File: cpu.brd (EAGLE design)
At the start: 94 x 46.5 mm, 87 parts, among them U1 STM32L151R8T6, X1 ED060SC4_EINK, X2 PIIKKIRIMA-5, X3 PIIKKIRIMA-2, X4 629105136821, X5 693071010811, X6 PIIKKIRIMA-6, X7 PIIKKIRIMA-2, X8 PIIKKIRIMA-2, X9 PIIKKIRIMA-2

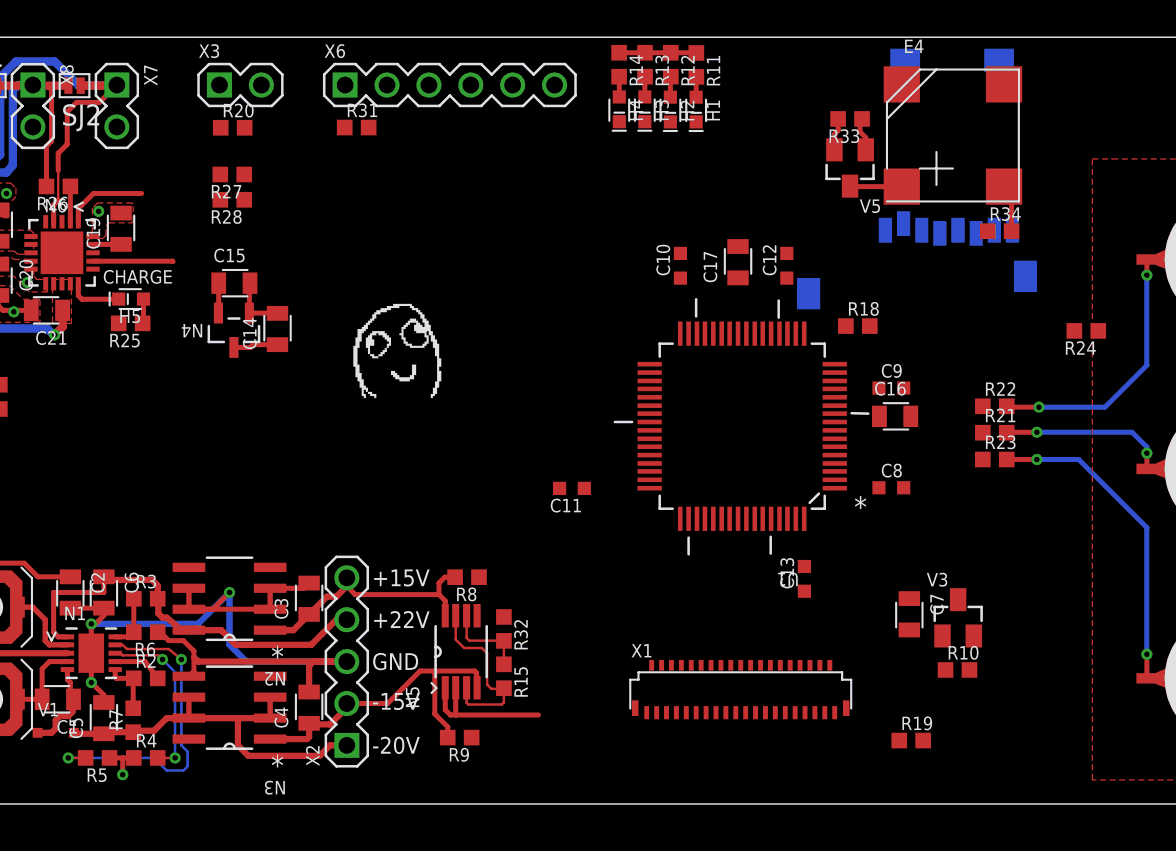
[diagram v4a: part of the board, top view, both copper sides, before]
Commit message: Layout cont
Flex connector first routing attempt. not nice. too many vias...
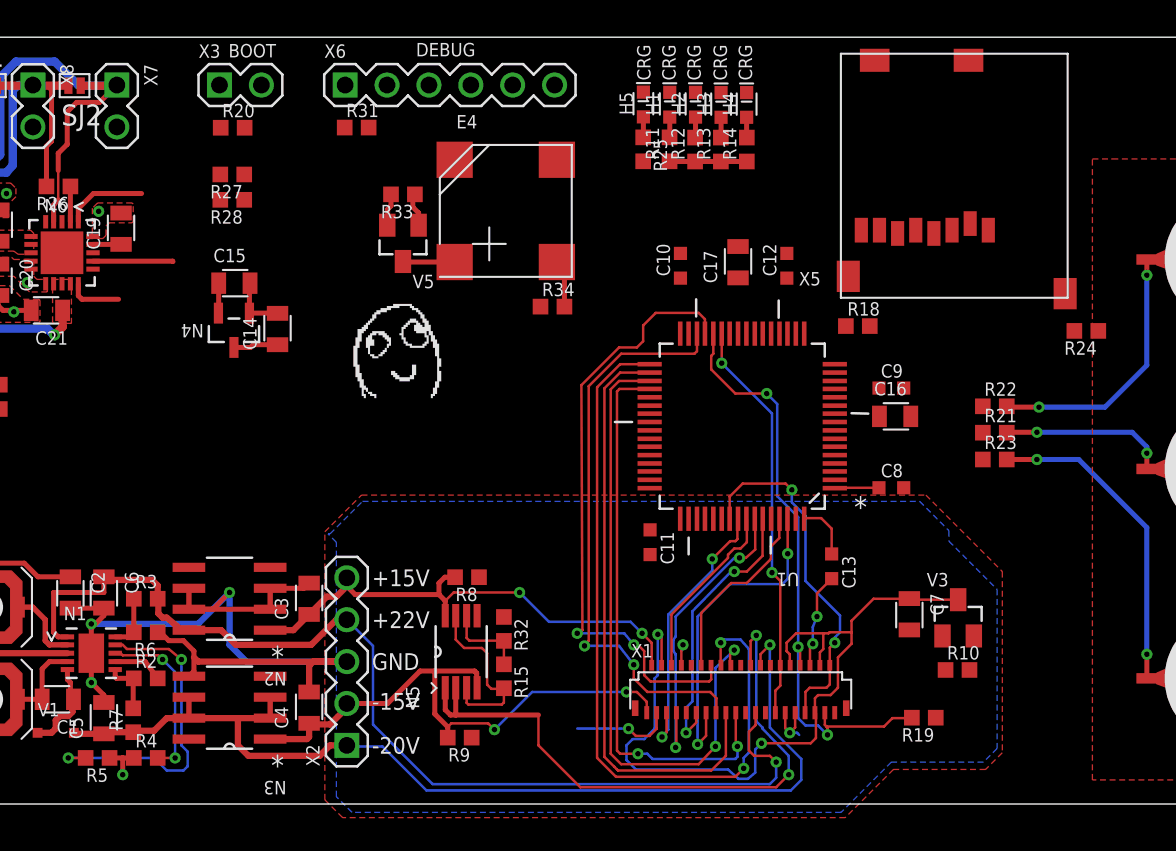
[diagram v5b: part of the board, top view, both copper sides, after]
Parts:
- moved H5 33.2 mm to (58.4, 45.0), turned to 90 degrees
- moved R25 32.8 mm to (58.4, 42.2), turned to 270 degrees
- moved R34 27.5 mm to (52.9, 32.7)
- moved R33 27.5 mm to (43.8, 39.5)
- moved V5 27.5 mm to (43.8, 36.5)
- moved E4 27.5 mm to (50.0, 38.5)
- moved R14 9.30 mm to (64.6, 42.2), turned to 90 degrees
- moved H4 7.73 mm to (64.6, 44.9), turned to 90 degrees
- moved R13 6.90 mm to (63.1, 42.2), turned to 90 degrees
- moved X5 6.24 mm to (79.3, 37.3), flipped to the top
- moved C11 5.75 mm to (58.8, 18.4), turned to 270 degrees
- moved R11 5.37 mm to (60.0, 42.2), turned to 90 degrees
- moved R12 5.35 mm to (61.5, 42.2), turned to 90 degrees
- moved H3 4.63 mm to (63.1, 44.9), turned to 90 degrees
- moved C13 1.82 mm to (69.8, 17.0), turned to 270 degrees
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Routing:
- net VEINK33: track 0.00 -> 47.8 mm, vias 0 -> 2
- net EINKD4: track 0.00 -> 46.6 mm, vias 0 -> 2
- net VNEG20: track 23.6 -> 63.1 mm, vias 0 -> 1
- net EINKD6: track 0.00 -> 39.1 mm, vias 0 -> 2
- net VPOS22: track 26.6 -> 65.0 mm, vias 0 -> 1
- net EINKD2: track 0.00 -> 37.3 mm, vias 0 -> 2
- net SPV/BOOT1: track 0.00 -> 36.8 mm, vias 0 -> 3
- net EINKD5: track 0.00 -> 36.2 mm
- net EINKD3: track 0.00 -> 35.1 mm, vias 0 -> 2
- net EINKD7: track 0.00 -> 34.1 mm, vias 0 -> 2
- net VEINKVCOM: track 8.77 -> 38.3 mm, vias 0 -> 2
- net GMODE: track 0.00 -> 24.6 mm, vias 0 -> 2
- net CKV: track 0.00 -> 21.8 mm, vias 0 -> 2
- net EINKD1: track 0.00 -> 19.9 mm, vias 0 -> 2
- net OE: track 0.00 -> 18.5 mm, vias 0 -> 2
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- added copper zone on layer 16, net GND
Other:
- board text added: "BOOT"
- board text added: "CRG"
- board text added: "DEBUG"
- board text removed: "CHARGE"

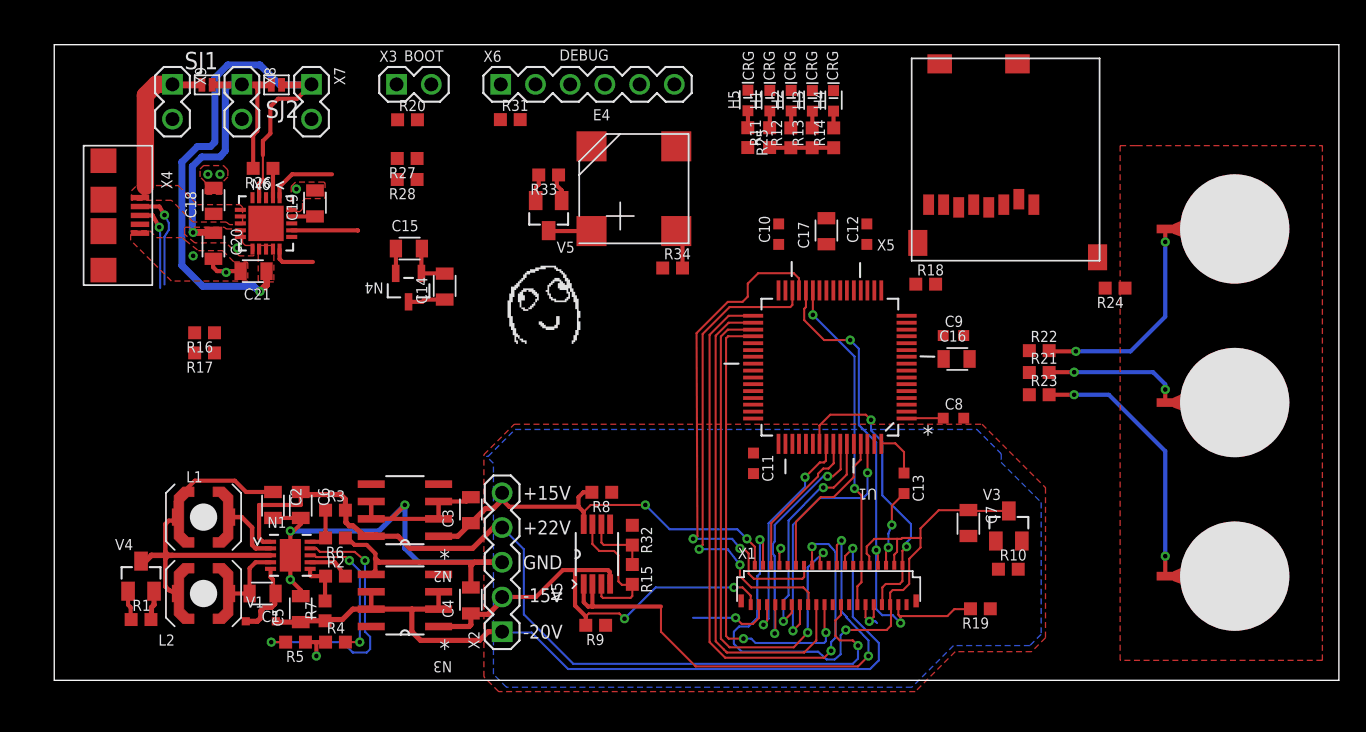
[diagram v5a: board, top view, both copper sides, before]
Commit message: Layout cont2
17 airwires left.
touch buttons removed from cpu board
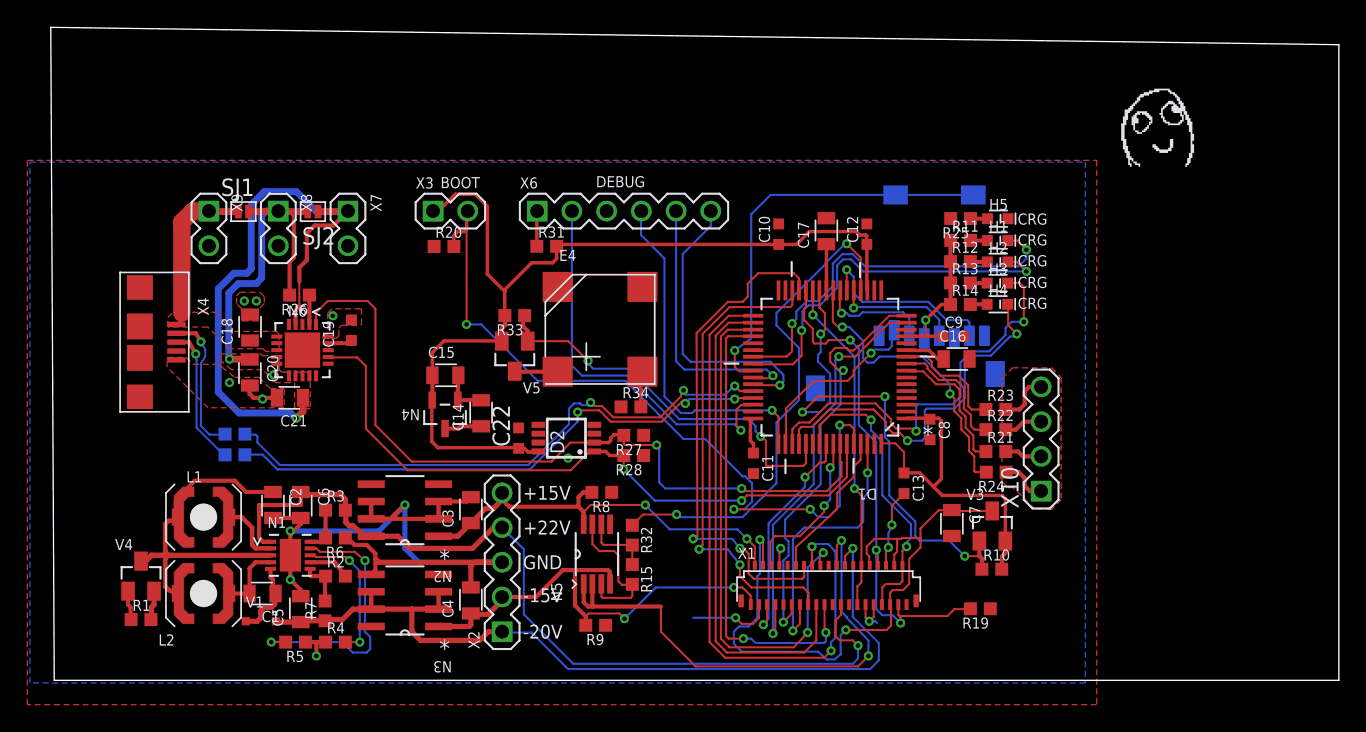
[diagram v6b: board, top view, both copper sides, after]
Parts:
- removed E1, E2, E3: TB_ROUND, OMAT_IC:TB_8MM_ROUND
- removed R18: 22R, rcl:R0603
- added C22: (no value), rcl:C0603
- added D2: TMP75DGK, ti_tmp:MSOP8
- added X10: PIIKKIRIMA-4, OMAT_IC:PIIKKIRIMA-4
- C19: device rcl:C0805 -> rcl:C0603
- moved U$2 46.7 mm to (88.5, 42.7)
- moved R27 26.2 mm to (50.0, 20.5)
- moved R28 26.1 mm to (50.0, 19.0)
- moved H5 20.2 mm to (76.6, 36.3), turned to 0 degrees
- moved H1 19.6 mm to (76.6, 34.7), turned to 0 degrees
- moved H2 19.2 mm to (76.6, 33.1), turned to 0 degrees
- moved H4 19.1 mm to (76.6, 30.0), turned to 0 degrees
- moved H3 19.0 mm to (76.6, 31.6), turned to 0 degrees
- moved R25 16.7 mm to (73.9, 36.3), turned to 180 degrees
- moved R24 16.0 mm to (76.5, 17.8)
- moved R11 15.9 mm to (73.9, 34.7), turned to 0 degrees
- moved R12 15.4 mm to (73.9, 33.2), turned to 0 degrees
- moved R14 15.3 mm to (73.9, 30.0), turned to 0 degrees
- moved R13 15.2 mm to (73.9, 31.6), turned to 0 degrees
- moved X5 14.8 mm to (68.0, 27.7), flipped to the bottom
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- renumbered U1 to D1
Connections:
- net N$12 renamed LED1
- net N$14 renamed LED2
- net N$16 renamed LED3
- net N$19 renamed LED4
- removed net STSCK1: D1.21, R18.1
- net +3V3: now also C22.1, D2.8
- net GND: now also C22.2, D2.4, D2.5, D2.6, D2.7
- net OE: now also D1.15; no longer D1.58
- net SCK1: now also D1.21; no longer R18.2
- net SCL: now also D1.58, D2.2
- net SDA: now also D1.59, D2.1
- net SPH: now also D1.16; no longer D1.59
- net TB1: now also X10.2; no longer E1.1
- net TB2: now also X10.3; no longer E2.1
- net TB3: now also X10.4; no longer E3.1
- net TBSHIELD: now also X10.1
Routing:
- net +3V3: track 14.6 -> 108.2 mm, vias 0 -> 1
- net BOOT0: track 0.00 -> 55.3 mm, vias 0 -> 4
- net SCL: track 5.01 -> 56.8 mm, vias 0 -> 2
- net SDA: track 4.86 -> 49.9 mm, vias 0 -> 2
- net USBDM: track 0.00 -> 43.1 mm, vias 0 -> 3
- net USBDP: track 0.00 -> 41.0 mm, vias 0 -> 3
- net DACOUT1: track 0.00 -> 36.9 mm, vias 0 -> 2
- net EINKVDDCTRLN: track 0.00 -> 36.3 mm, vias 0 -> 4
- net USD_DETN: track 0.00 -> 30.1 mm, vias 0 -> 1
- net LED3: track 0.00 -> 29.9 mm, vias 0 -> 2
- net SWDIO: track 0.00 -> 28.6 mm, vias 0 -> 1
- net LED1: track 0.00 -> 28.5 mm, vias 0 -> 2
- net LED2: track 0.00 -> 28.0 mm, vias 0 -> 2
- net LED4: track 0.00 -> 27.1 mm, vias 0 -> 2
- net BUZCTRLN: track 2.07 -> 29.1 mm, vias 0 -> 2
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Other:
- board size 94 x 46.5 mm -> 94.2 x 47.8 mm

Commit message: Layout complete
First completed layout , Airwires 0
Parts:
- moved U$2 66.5 mm to (23.8, 27.2)
- moved R1 12.6 mm to (2.86, 12.8), turned to 180 degrees
- moved C12 11.3 mm to (56.1, 32.5)
- moved C7 11.3 mm to (62.3, 11.4)
- moved C9 11.3 mm to (62.4, 25.0)
- moved C10 11.3 mm to (49.6, 32.5)
- moved C13 11.3 mm to (58.8, 14.3)
- moved C15 11.3 mm to (25.2, 22.2)
- moved C17 11.3 mm to (53.1, 32.7)
- moved C19 11.3 mm to (18.4, 25.5)
- moved C22 11.3 mm to (30.6, 17.6)
- moved C3 11.3 mm to (27.1, 12.3)
- moved C4 11.3 mm to (27.1, 5.71)
- moved C8 11.3 mm to (60.7, 18.2)
- moved D1 11.3 mm to (53.4, 22.8)
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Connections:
- net +3V3: now also R25.2
- net VSYS: no longer R25.2
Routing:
- net +3V3: track 108.2 -> 184.0 mm, vias 1 -> 7
- net N$20: track 0.00 -> 63.2 mm, vias 0 -> 2
- net RESETN: track 2.59 -> 44.2 mm, vias 0 -> 1
- net VSYS: track 31.6 -> 67.6 mm, vias 2 -> 4
- net GND: track 84.5 -> 92.9 mm, vias 15 -> 110
- net G8IO4: track 2.98 -> 5.52 mm
- net SCL: track 56.8 -> 58.6 mm
- net NSS1: track 13.7 -> 15.0 mm
- net LED2: track 28.0 -> 29.2 mm
- net BOOT0: track 55.3 -> 56.0 mm
- net LE: track 11.9 -> 12.5 mm
- net EINKD1: track 20.4 -> 20.9 mm
- added copper zone on layer 16, net N$12
- removed copper zone on layer 16, net GND
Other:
- board size 94.2 x 47.8 mm -> 72.4 x 38.1 mm
- board text added: "Act"
- board text added: "Chg"
- board text added: "Dbg"
- board text added: "EINK"
- board text added: "Flip"
- board text added: "KL 2013"
- board text added: "Run"
- board text removed: "CRG"

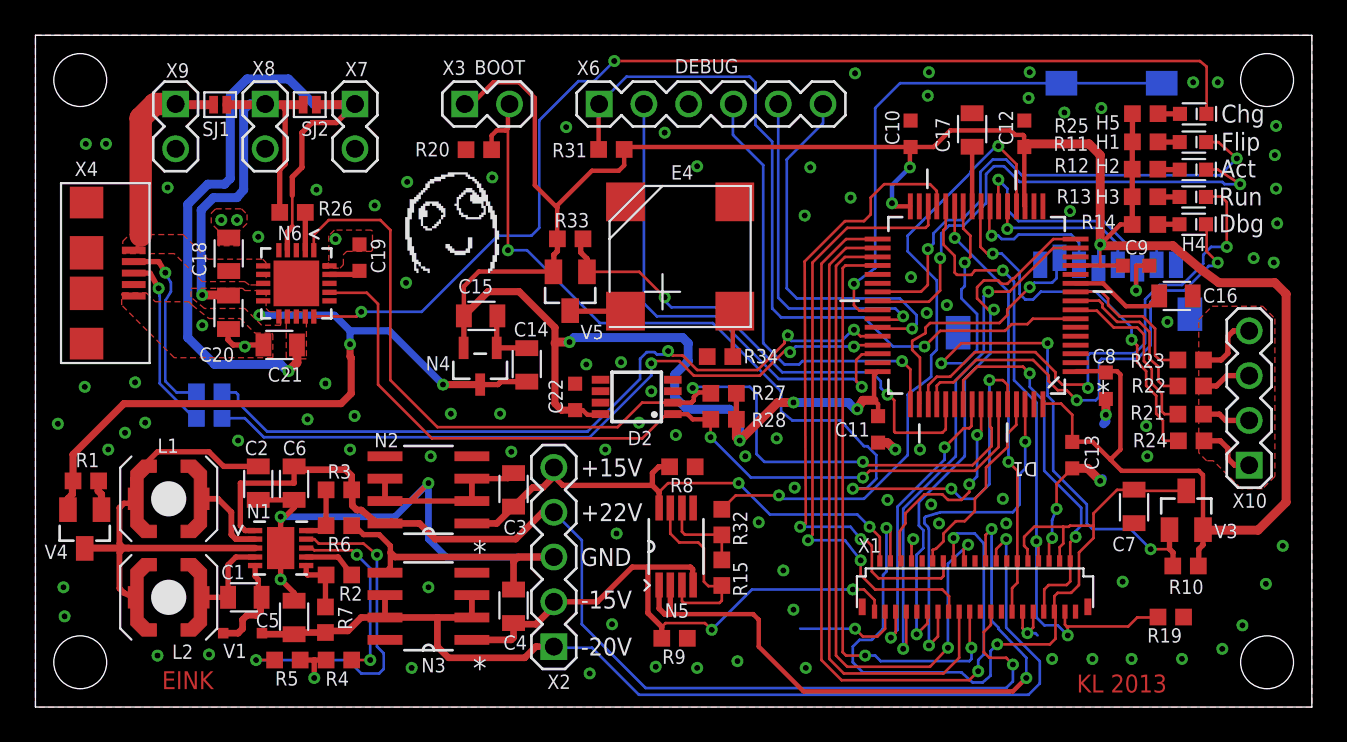
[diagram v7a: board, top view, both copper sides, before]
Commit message: Finetuning
USB connector moved closer to edge etc.
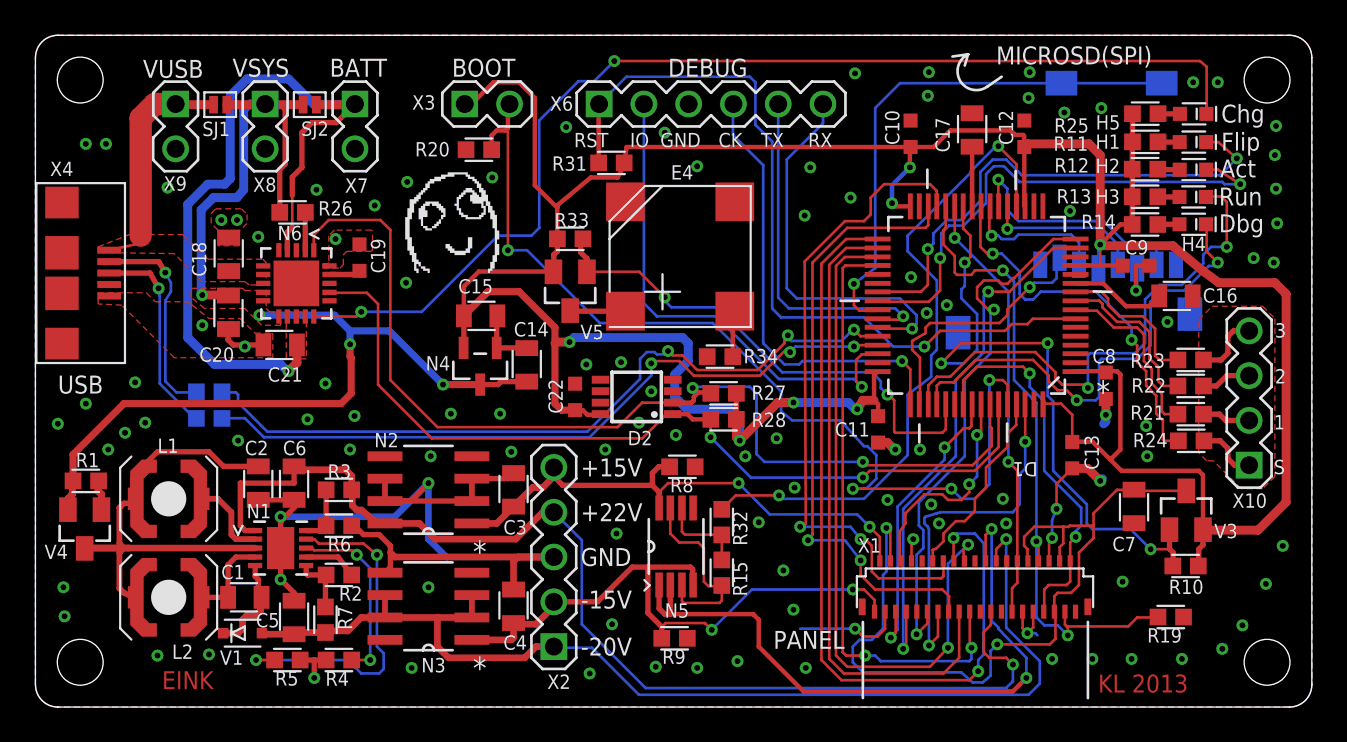
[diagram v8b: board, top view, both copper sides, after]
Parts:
- moved X4 1.40 mm to (4.18, 24.6)
- moved R31 0.76 mm to (32.7, 30.9)
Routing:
- net N$4: track 10.5 -> 11.9 mm
- net N$2: track 10.2 -> 11.6 mm
- net VUSB: track 12.1 -> 13.4 mm
- net RESETN: track 44.2 -> 45.0 mm
- added copper zone on layer 16, net GND
- removed copper zone on layer 16, net N$12
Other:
- outline, holes or cut-outs redrawn
- board text added: "1"
- board text added: "2"
- board text added: "3"
- board text added: "BATT"
- board text added: "CK"
- board text added: "IO"
- board text added: "MICROSD(SPI)"
- board text added: "PANEL"
- board text added: "RST"
- board text added: "RX"
- board text added: "S"
- board text added: "TX"
- board text added: "USB"
- board text added: "VSYS"
- board text added: "VUSB"
- board text added: "eInk Display Controler V1.0 KL 12.9.2013"
